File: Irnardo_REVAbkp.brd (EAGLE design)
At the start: 12 x 17 mm, 20 parts, among them J1 USB_PAD, U1 ATMEGA32U4-MU, U2 TSOP755, X1 16MHz

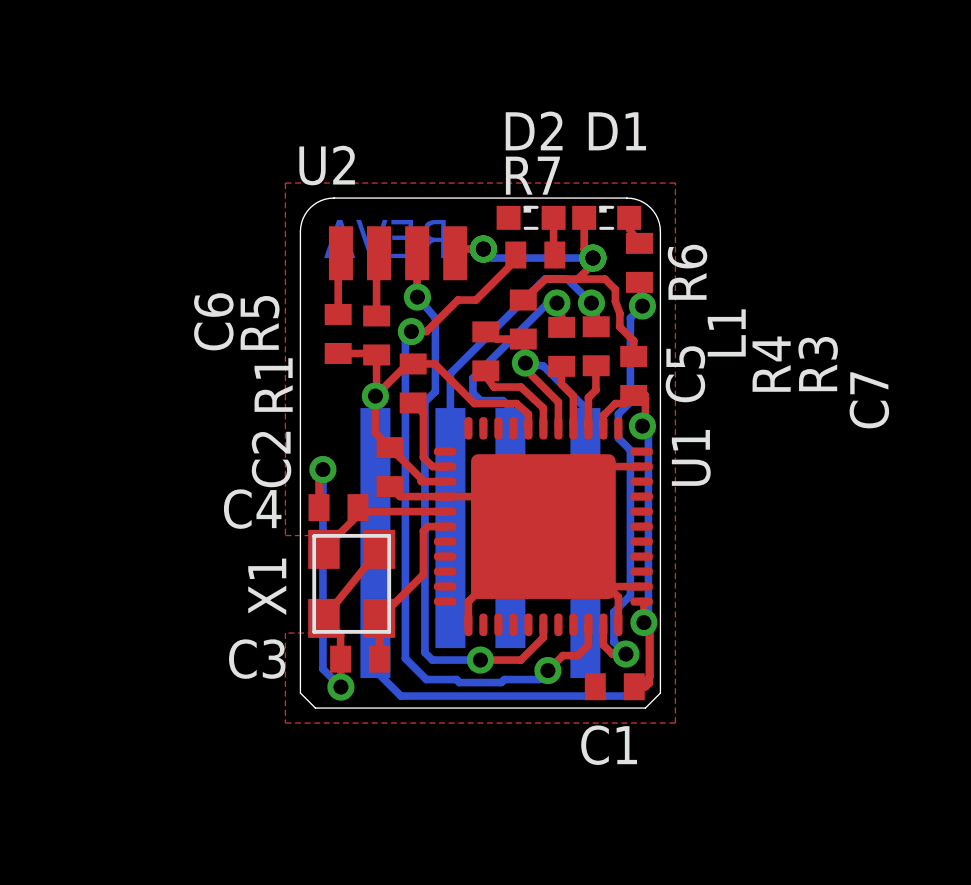
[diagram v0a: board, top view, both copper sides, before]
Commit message: Fix de-couple cap on IR receiver
C6 de-coupling U2 was wrong side of R5.
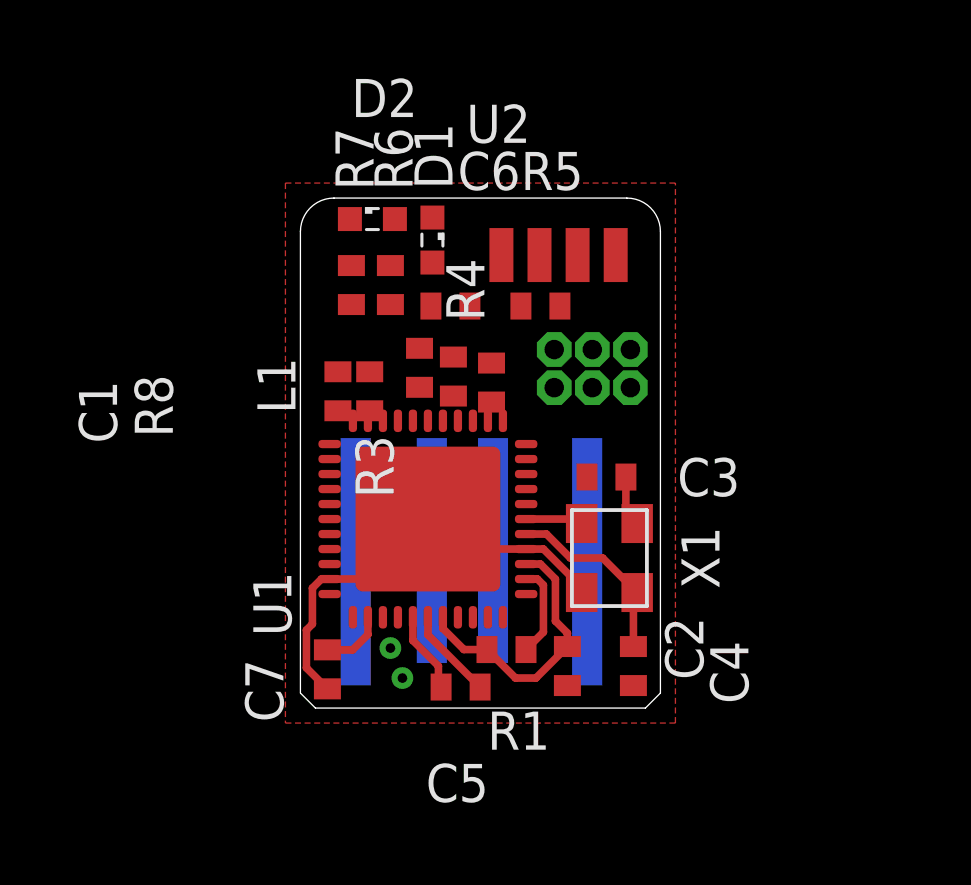
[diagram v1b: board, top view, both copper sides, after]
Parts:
- added R8: 10K, resistor:R0402
- J1: value USB_PAD -> ICSP; device USB_PAD:USB_PAD -> 6X2005IN:6X2005IN
- moved C7 14.1 mm to (0.90, 1.29), turned to 270 degrees
- moved C1 13.5 mm to (1.25, 10.6), turned to 90 degrees
- moved J1 11.3 mm to (9.73, 10.7), flipped to the top
- moved C5 11.2 mm to (5.34, 0.70), turned to 180 degrees
- moved C4 11.2 mm to (11.1, 1.40), turned to 270 degrees
- moved C3 10.2 mm to (10.2, 7.70), turned to 0 degrees
- moved R1 9.40 mm to (6.87, 1.95), turned to 0 degrees
- moved C2 8.88 mm to (8.90, 1.40)
- moved X1 8.63 mm to (10.3, 5.00), turned to 270 degrees
- moved R6 8.33 mm to (3.00, 14.1)
- moved R7 6.21 mm to (1.70, 14.1), turned to 90 degrees
- moved R3 5.93 mm to (3.97, 11.3), turned to 90 degrees
- moved D1 5.86 mm to (4.40, 15.6), turned to 270 degrees
- moved R5 5.55 mm to (8.00, 13.4), turned to 180 degrees
- moved U2 5.35 mm to (6.70, 15.1)
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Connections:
- new net N$9: R8.1, U1.33
- net +5V: now also J1.2; no longer J1.V+
- net D+: no longer J1.D+
- net D-: no longer J1.D-
- net GND: now also J1.6, R8.2; no longer U1.33
- net MISO: now also J1.1
- net MOSI: now also J1.4
- net RESET: now also J1.5
- net SCK: now also J1.3
- net UGND: no longer J1.V-
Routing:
- net +5V: track 47.7 -> 11.4 mm, vias 3 -> 0
- net GND: track 49.5 -> 16.5 mm, vias 4 -> 0
- net IO5: track 23.2 -> 0.00 mm, vias 2 -> 0
- net IO8: track 18.5 -> 0.00 mm, vias 2 -> 0
- net IO13: track 14.8 -> 0.00 mm, vias 2 -> 0
- net D-: track 12.3 -> 0.00 mm, vias 1 -> 0
- net D+: track 10.7 -> 0.00 mm, vias 1 -> 0
- net UGND: track 11.9 -> 2.71 mm, vias 1 -> 0
- net N$1: track 5.67 -> 1.91 mm
- net RD+: track 2.23 -> 0.00 mm
- net RD-: track 2.19 -> 0.00 mm
- net N$5: track 2.12 -> 0.00 mm
- net N$2: track 4.82 -> 6.36 mm
- net N$7: track 1.26 -> 0.00 mm
- net N$8: track 0.96 -> 0.00 mm
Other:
- board text removed: "REVA"
